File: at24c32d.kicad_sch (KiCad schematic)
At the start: 10 parts, among them J1901 961102-6404-AR, U1901 AT24C64D-SSHM-T

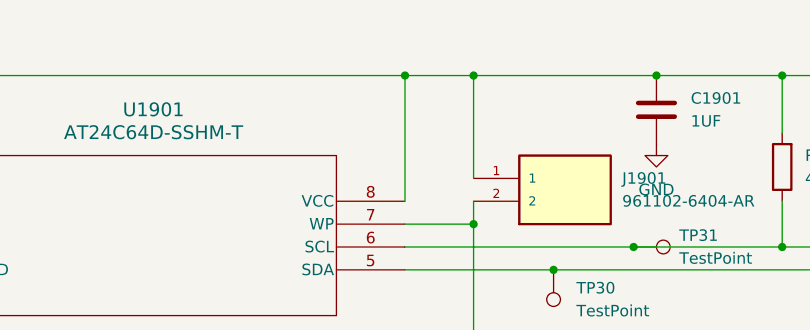
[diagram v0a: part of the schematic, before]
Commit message: Updates from Michal to fix ERC errors
Still lots of ERC warnings
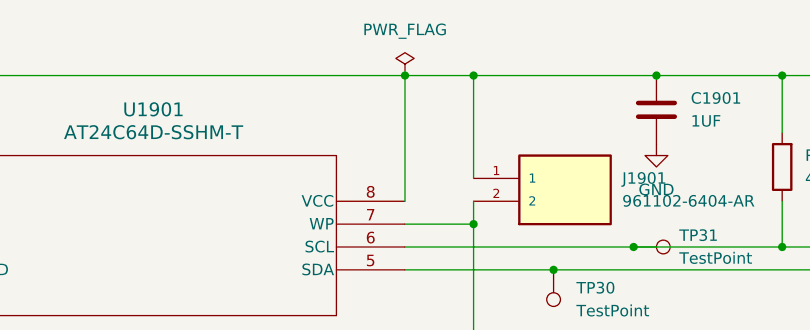
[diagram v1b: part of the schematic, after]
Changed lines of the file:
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@@
+	)
+	(symbol
+		(lib_id "power:PWR_FLAG")
+		(at 185.42 64.77 0)
+		(unit 1)
+		(exclude_from_sim no)
+		(in_bom yes)
+		(on_board yes)
+		(dnp no)
+		(fields_autoplaced yes)
+		(property "Reference" "#FLG09"
+			(at 185.42 62.865 0)
+			(effects
+				(font
+					(size 1.27 1.27)
+				)
+				(hide yes)
+			)
+		)
+		(property "Value" "PWR_FLAG"
+			(at 185.42 59.69 0)
+			(effects
+				(font
+					(size 1.27 1.27)
+				)
+			)
+		)
+		(property "Footprint" ""
+			(at 185.42 64.77 0)
+			(effects
+				(font
+					(size 1.27 1.27)
+				)
+				(hide yes)
+			)
+		)
+		(property "Datasheet" "~"
+			(at 185.42 64.77 0)
+			(effects
+				(font
+					(size 1.27 1.27)
+				)
+				(hide yes)
+			)
+		)
+		(property "Description" "Special symbol for telling ERC where power comes from"
+			(at 185.42 64.77 0)
+			(effects
+				(font
+					(size 1.27 1.27)
+				)
+				(hide yes)
+			)
+		)
+		(pin "1"
+		)
+		(instances
+			(project "zest"
+				(path "/00000000-0000-0000-0000-000000000003/00000000-0000-0000-0000-00000000000e"
+					(reference "#FLG09")
+					(unit 1)
+				)
+			)
+		)
 	)
 	(symbol

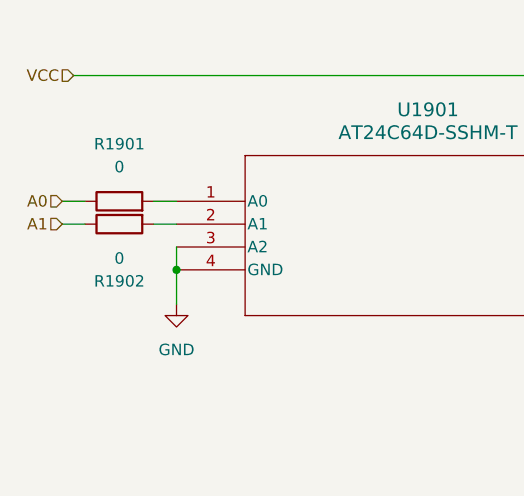
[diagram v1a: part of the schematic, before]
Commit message: Schematic Changes
Added Manufacturer/MPN/Description Fields to parts
Added libraries to project
Modified FMC schematic to use new symbol
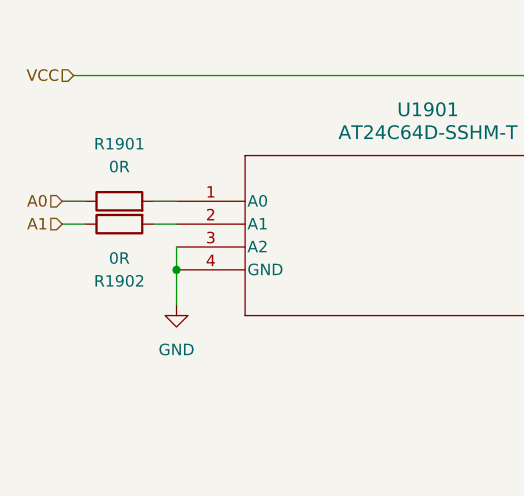
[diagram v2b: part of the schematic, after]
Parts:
- C1901: Manufacturer (none) -> Murata; Manufacturer Part Number (none) -> GRM188R61E105KA12D
- J1901: Manufacturer (none) -> 3M; Manufacturer Part Number (none) -> 3M9447-ND
- R1901, R1902: value 0 -> 0R; Manufacturer (none) -> Panasonic; Manufacturer Part Number (none) -> ERJ-3GEY0R00V
- R1903: Manufacturer (none) -> YAGEO; Manufacturer Part Number (none) -> RC0603FR-0711K5L
- R1904, R1905: Manufacturer (none) -> YAGEO; Manufacturer Part Number (none) -> RC0603FR-074K75L
- U1901: Manufacturer (none) -> Microchip Technology; Manufacturer Part Number (none) -> AT24C64D-SSHM-T
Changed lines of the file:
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@@
 			)
 		)
-		(property "Description" "Resistor"
+		(property "Description" "RES 11.5K OHM 1% 1/10W 0603"
 			(at 193.04 104.14 0)
 			(effects
@@
 		(property "Vendor" "digikey:311-11.5KHRCT-ND"
 			(at 386.08 0 0)
+			(effects
+				(font
+					(size 1.27 1.27)
+				)
+				(hide yes)
+			)
+		)
+		(property "Manufacturer" "YAGEO "
+			(at 193.04 104.14 0)
+			(effects
+				(font
+					(size 1.27 1.27)
+				)
+				(hide yes)
+			)
+		)
+		(property "Manufacturer Part Number" "RC0603FR-0711K5L "
+			(at 193.04 104.14 0)
 			(effects
 				(font
@@
 			)
 		)
+		(property "Manufacturer" ""
+			(at 201.93 86.36 0)
+			(effects
+				(font
+					(size 1.27 1.27)
+				)
+				(hide yes)
+			)
+		)
+		(property "Manufacturer Part Number" ""
+			(at 201.93 86.36 0)
+			(effects
+				(font
+					(size 1.27 1.27)
+				)
+				(hide yes)
+			)
+		)
 		(pin "1"
 		)
@@
 			)
 		)
-		(property "Description" "Unpolarized capacitor"
+		(property "Description" "CAP CER 1UF 25V X5R 0603"
 			(at 213.36 68.58 0)
 			(effects
@@
 		(property "Vendor" "digikey:490-3897-1-ND"
 			(at 0 137.16 0)
+			(effects
+				(font
+					(size 1.27 1.27)
+				)
+				(hide yes)
+			)
+		)
+		(property "Manufacturer" "Murata"
+			(at 213.36 68.58 0)
+			(effects
+				(font
+					(size 1.27 1.27)
+				)
+				(hide yes)
+			)
+		)
+		(property "Manufacturer Part Number" "GRM188R61E105KA12D"
+			(at 213.36 68.58 0)
 			(effects
 				(font
@@
 			)
 		)
-		(property "Description" ""
+		(property "Description" "IC EEPROM 64KBIT I2C 1MHZ 8SOIC"
 			(at 129.54 78.74 0)
 			(effects
@@
 		(property "Vendor" "digikey:AT24C64D-SSHM-TCT-ND"
 			(at 0 157.48 0)
+			(effects
+				(font
+					(size 1.27 1.27)
+				)
+				(hide yes)
+			)
+		)
+		(property "Manufacturer" "Microchip Technology "
+			(at 129.54 78.74 0)
+			(effects
+				(font
+					(size 1.27 1.27)
+				)
+				(hide yes)
+			)
+		)
+		(property "Manufacturer Part Number" "AT24C64D-SSHM-T "
+			(at 129.54 78.74 0)
 			(effects
 				(font
@@
 			)
 		)
-		(property "Description" "Resistor"
+		(property "Description" "RES 4.75K OHM 1% 1/10W 0603"
 			(at 233.68 74.93 0)
 			(effects
@@
 		(property "Vendor" "digikey:311-4.75KHRCT-ND"
 			(at 467.36 0 0)
+			(effects
+				(font
+					(size 1.27 1.27)
+				)
+				(hide yes)
+			)
+		)
+		(property "Manufacturer" "YAGEO "
+			(at 233.68 74.93 0)
+			(effects
+				(font
+					(size 1.27 1.27)
+				)
+				(hide yes)
+			)
+		)
+		(property "Manufacturer Part Number" "RC0603FR-074K75L "
+			(at 233.68 74.93 0)
 			(effects
 				(font
@@
 			)
 		)
-		(property "Description" "Connector Header Through Hole 2 position 0.100 (2.54mm)"
+		(property "Description" "CONN HEADER VERT 2POS 2.54MM"
 			(at 200.66 78.74 0)
 			(effects
@@
 		(property "Vendor" "digikey:3M9447-ND"
 			(at 0 157.48 0)
+			(effects
+				(font
+					(size 1.27 1.27)
+				)
+				(hide yes)
+			)
+		)
+		(property "Manufacturer" "3M "
+			(at 200.66 78.74 0)
+			(effects
+				(font
+					(size 1.27 1.27)
+				)
+				(hide yes)
+			)
+		)
+		(property "Manufacturer Part Number" "3M9447-ND "
+			(at 200.66 78.74 0)
 			(effects
 				(font
@@
 			)
 		)
-		(property "Value" "0"
+		(property "Value" "0R"
 			(at 123.19 74.93 90)
 			(effects
@@
 			)
 		)
-		(property "Description" "Resistor"
+		(property "Description" "RES SMD 0 OHM JUMPER 1/10W 0603"
 			(at 123.19 78.74 0)
 			(effects
@@
 		(property "Vendor" "digikey:P0.0GCT-ND"
 			(at 201.93 201.93 0)
+			(effects
+				(font
+					(size 1.27 1.27)
+				)
+				(hide yes)
+			)
+		)
+		(property "Manufacturer" "Panasonic"
+			(at 123.19 78.74 0)
+			(effects
+				(font
+					(size 1.27 1.27)
+				)
+				(hide yes)
+			)
+		)
+		(property "Manufacturer Part Number" "ERJ-3GEY0R00V "
+			(at 123.19 78.74 0)
 			(effects
 				(font
@@
 			)
 		)
-		(property "Description" "Resistor"
+		(property "Description" "RES 4.75K OHM 1% 1/10W 0603"
 			(at 227.33 74.93 0)
 			(effects
@@
 		(property "Vendor" "digikey:311-4.75KHRCT-ND"
 			(at 454.66 0 0)
+			(effects
+				(font
+					(size 1.27 1.27)
+				)
+				(hide yes)
+			)
+		)
+		(property "Manufacturer" "YAGEO "
+			(at 227.33 74.93 0)
+			(effects
+				(font
+					(size 1.27 1.27)
+				)
+				(hide yes)
+			)
+		)
+		(property "Manufacturer Part Number" "RC0603FR-074K75L "
+			(at 227.33 74.93 0)
 			(effects
 				(font
@@
 			)
 		)
-		(property "Value" "0"
+		(property "Value" "0R"
 			(at 123.19 85.09 90)
 			(effects
@@
 			)
 		)
-		(property "Description" "Resistor"
+		(property "Description" "RES SMD 0 OHM JUMPER 1/10W 0603"
 			(at 123.19 81.28 0)
 			(effects
@@
 		(property "Vendor" "digikey:P0.0GCT-ND"
 			(at 204.47 -41.91 0)
+			(effects
+				(font
+					(size 1.27 1.27)
+				)
+				(hide yes)
+			)
+		)
+		(property "Manufacturer" "Panasonic"
+			(at 123.19 81.28 0)
+			(effects
+				(font
+					(size 1.27 1.27)
+				)
+				(hide yes)
+			)
+		)
+		(property "Manufacturer Part Number" "ERJ-3GEY0R00V "
+			(at 123.19 81.28 0)
 			(effects
 				(font
@@
 			(at 210.82 83.82 0)
 			(effects
+				(font
+					(size 1.27 1.27)
+				)
+				(hide yes)
+			)
+		)
+		(property "Manufacturer" ""
+			(at 210.82 83.82 0)
+			(effects
+				(font
+					(size 1.27 1.27)
+				)
+				(hide yes)
+			)
+		)
+		(property "Manufacturer Part Number" ""
+			(at 210.82 83.82 0)
+			(effects

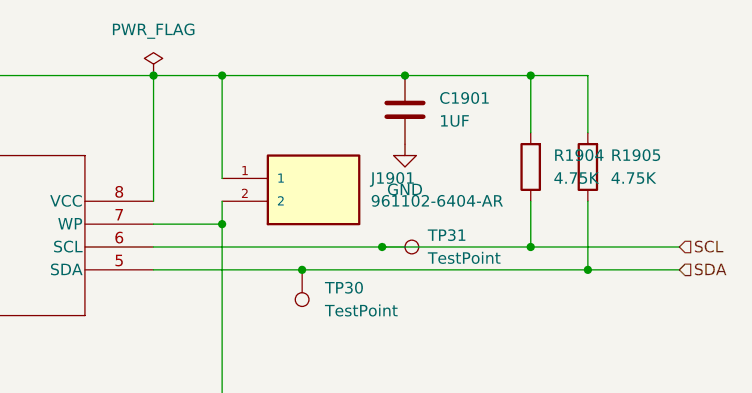
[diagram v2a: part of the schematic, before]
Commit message: Schematics update
Cleaned up RF ADC and front end sections.
Verified that changes did not changes anything about the layout.
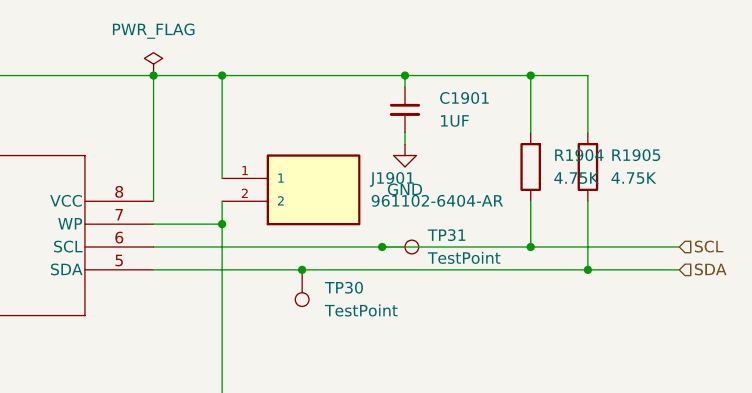
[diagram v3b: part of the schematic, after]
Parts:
- C1901: symbol Device:C -> Device:C_Small
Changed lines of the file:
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@@
+	)
+	(junction
+		(at 213.36 64.77)
+		(diameter 0)
+		(color 0 0 0 0)
 	)
 	(junction
@@
 	)
 	(junction
-		(at 213.36 64.77)
-		(diameter 0)
-		(color 0 0 0 0)
-	)
-	(junction
 		(at 210.82 83.82)
 		(diameter 0)
@@
 	(wire
 		(pts
+			(xy 185.42 64.77) (xy 193.04 64.77)
+		)
+		(stroke
+			(width 0)
+			(type default)
+		)
+	)
+	(wire
+		(pts
 			(xy 213.36 64.77) (xy 227.33 64.77)
 		)
@@
 	(wire
 		(pts
-			(xy 185.42 64.77) (xy 193.04 64.77)
-		)
-		(stroke
-			(width 0)
-			(type default)
-		)
-	)
-	(wire
-		(pts
 			(xy 227.33 78.74) (xy 227.33 83.82)
 		)
@@
 	(wire
 		(pts
+			(xy 213.36 64.77) (xy 213.36 66.04)
+		)
+		(stroke
+			(width 0)
+			(type default)
+		)
+	)
+	(wire
+		(pts
 			(xy 233.68 86.36) (xy 201.93 86.36)
+		)
+		(stroke
+			(width 0)
+			(type default)
+		)
+	)
+	(wire
+		(pts
+			(xy 213.36 71.12) (xy 213.36 72.39)
 		)
 		(stroke
@@
 	)
 	(symbol
-		(lib_id "Device:C")
+		(lib_id "Device:C_Small")
 		(at 213.36 68.58 0)
 		(unit 1)
